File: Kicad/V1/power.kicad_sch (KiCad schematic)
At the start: 14 parts, among them U12 TPS2113APWR, U13 AMS1117

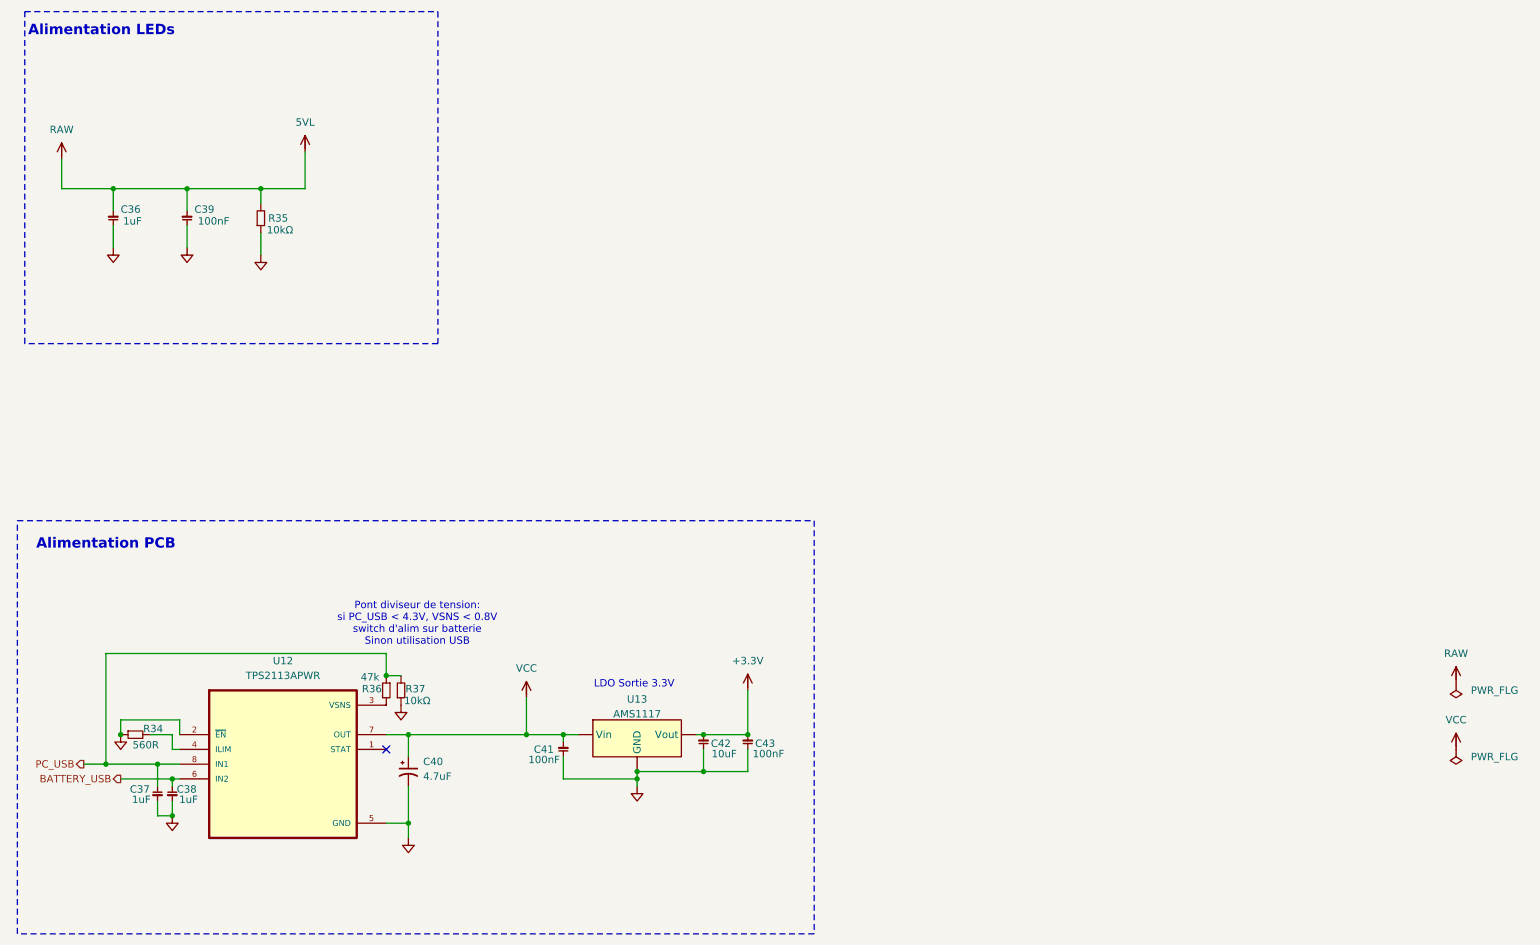
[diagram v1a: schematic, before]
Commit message: ERC almost done, footprint to assign
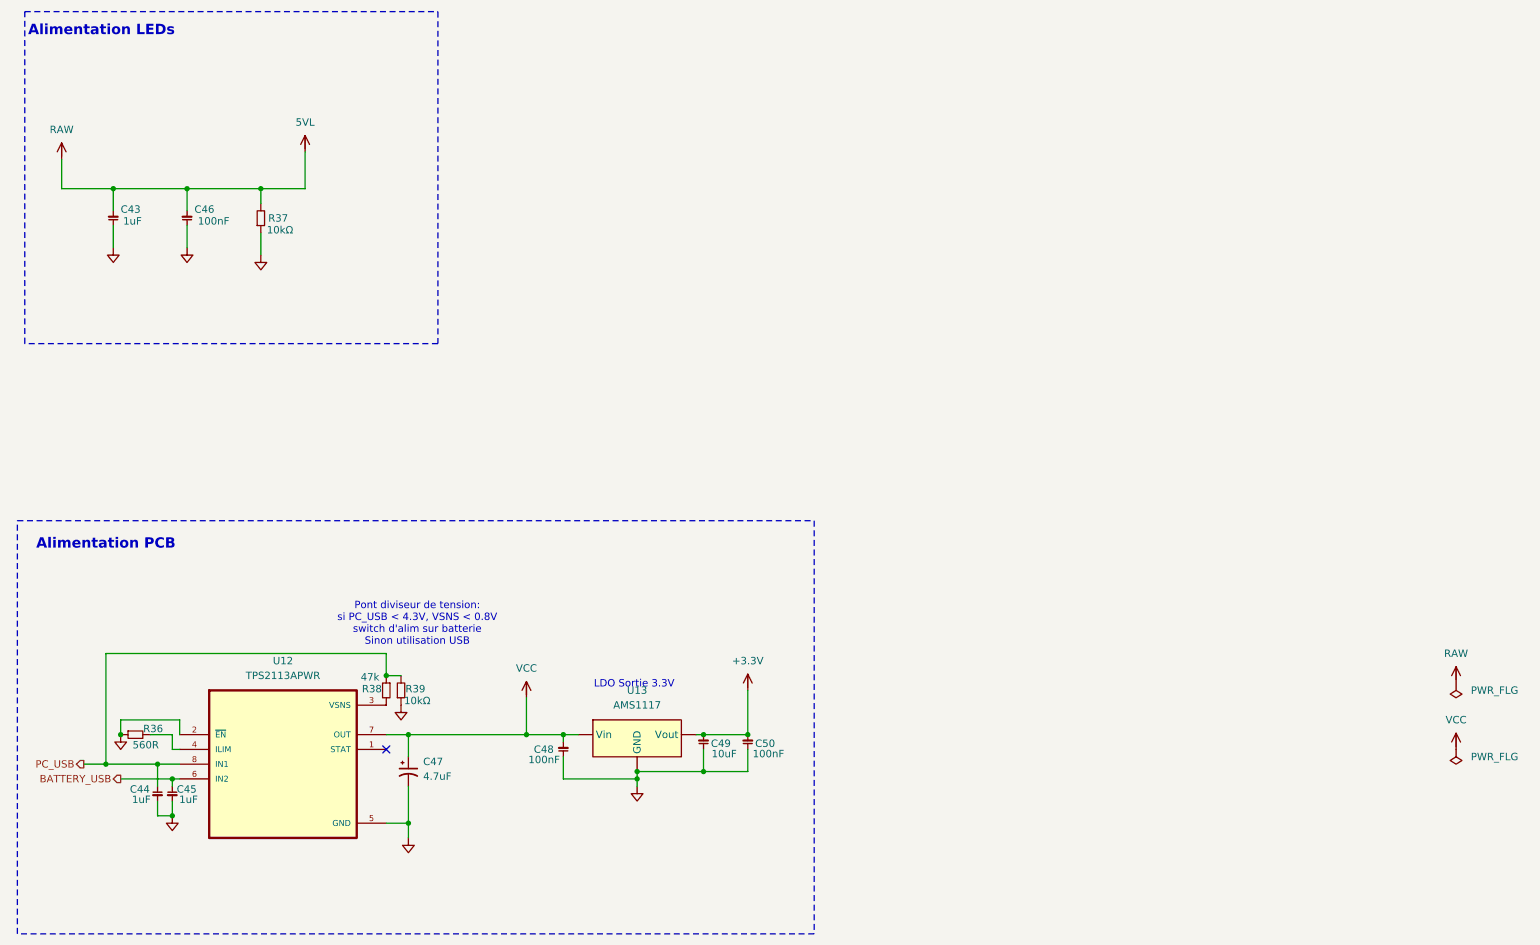
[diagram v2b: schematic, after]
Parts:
- U12: footprint MyGlove:TPS2113 -> TPS2113APWR:SOP65P640X120-8N; Price 2.67 -> None
- renumbered C36 to C43, C37 to C44, C38 to C45, C39 to C46, C40 to C47, C41 to C48, C42 to C49, C43 to C50, R34 to R36, R35 to R37, R36 to R38, R37 to R39

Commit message: ERC Check
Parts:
- U12: footprint TPS2113APWR:SOP65P640X120-8N -> MyGlove:TPS2113
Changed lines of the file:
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@@
 			)
 		)
-		(property "Footprint" "TPS2113APWR:SOP65P640X120-8N"
+		(property "Footprint" "MyGlove:TPS2113"
 			(at 69.85 158.75 0)
 			(hide yes)

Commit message: correction 328p et ajout d'un capa
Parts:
- renumbered C43 to C44, C44 to C45, C45 to C46, C46 to C47, C47 to C48, C48 to C49, C49 to C50, C50 to C51
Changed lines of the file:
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@@
 		(in_pos_files yes)
 		(dnp no)
-		(property "Reference" "C46"
+		(property "Reference" "C47"
 			(at 54.61 63.246 0)
 			(show_name no)
@@
 			(project "G-Love"
 				(path "/808bc5ea-49ac-4454-ba77-8b20d01ce159/0d387f9d-76d6-4b6a-aded-93bcda75ef5a/0a598795-0604-41b3-948f-4efe200200e3"
-					(reference "C46")
+					(reference "C47")
 					(unit 1)
 				)
@@
 		(in_pos_files yes)
 		(dnp no)
-		(property "Reference" "C49"
+		(property "Reference" "C50"
 			(at 143.51 155.194 0)
 			(show_name no)
@@
 			(project "G-Love"
 				(path "/808bc5ea-49ac-4454-ba77-8b20d01ce159/0d387f9d-76d6-4b6a-aded-93bcda75ef5a/0a598795-0604-41b3-948f-4efe200200e3"
-					(reference "C49")
+					(reference "C50")
 					(unit 1)
 				)
@@
 		(in_pos_files yes)
 		(dnp no)
-		(property "Reference" "C45"
+		(property "Reference" "C46"
 			(at 51.562 163.068 0)
 			(show_name no)
@@
 			(project "G-Love"
 				(path "/808bc5ea-49ac-4454-ba77-8b20d01ce159/0d387f9d-76d6-4b6a-aded-93bcda75ef5a/0a598795-0604-41b3-948f-4efe200200e3"
-					(reference "C45")
+					(reference "C46")
 					(unit 1)
 				)
@@
 		(dnp no)
 		(fields_autoplaced yes)
-		(property "Reference" "C47"
+		(property "Reference" "C48"
 			(at 93.98 158.3181 0)
 			(show_name no)
@@
 			(project "G-Love"
 				(path "/808bc5ea-49ac-4454-ba77-8b20d01ce159/0d387f9d-76d6-4b6a-aded-93bcda75ef5a/0a598795-0604-41b3-948f-4efe200200e3"
-					(reference "C47")
+					(reference "C48")
 					(unit 1)
 				)
@@
 		(in_pos_files yes)
 		(dnp no)
-		(property "Reference" "C48"
+		(property "Reference" "C49"
 			(at 113.03 156.21 0)
 			(show_name no)
@@
 			(project "G-Love"
 				(path "/808bc5ea-49ac-4454-ba77-8b20d01ce159/0d387f9d-76d6-4b6a-aded-93bcda75ef5a/0a598795-0604-41b3-948f-4efe200200e3"
-					(reference "C48")
+					(reference "C49")
 					(unit 1)
 				)
@@
 		(in_pos_files yes)
 		(dnp no)
-		(property "Reference" "C43"
+		(property "Reference" "C44"
 			(at 41.91 63.246 0)
 			(show_name no)
@@
 			(project "G-Love"
 				(path "/808bc5ea-49ac-4454-ba77-8b20d01ce159/0d387f9d-76d6-4b6a-aded-93bcda75ef5a/0a598795-0604-41b3-948f-4efe200200e3"
-					(reference "C43")
+					(reference "C44")
 					(unit 1)
 				)
@@
 		(in_pos_files yes)
 		(dnp no)
-		(property "Reference" "C44"
+		(property "Reference" "C45"
 			(at 45.212 163.068 0)
 			(show_name no)
@@
 			(project "G-Love"
 				(path "/808bc5ea-49ac-4454-ba77-8b20d01ce159/0d387f9d-76d6-4b6a-aded-93bcda75ef5a/0a598795-0604-41b3-948f-4efe200200e3"
-					(reference "C44")
+					(reference "C45")
 					(unit 1)
 				)
@@
 		(in_pos_files yes)
 		(dnp no)
-		(property "Reference" "C50"
+		(property "Reference" "C51"
 			(at 151.13 155.194 0)
 			(show_name no)
@@
 			(project "G-Love"
 				(path "/808bc5ea-49ac-4454-ba77-8b20d01ce159/0d387f9d-76d6-4b6a-aded-93bcda75ef5a/0a598795-0604-41b3-948f-4efe200200e3"
-					(reference "C50")
+					(reference "C51")
 					(unit 1)
 				)
